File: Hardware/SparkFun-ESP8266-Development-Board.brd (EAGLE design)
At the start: 55.3 x 25.9 mm, 70 parts, among them J1 U.FL, Q1 2.5A/30V, Q2 MMBT2222A, U1 ESP8266, U2 MCP73831, U3 AT25SF041-SOIC8, U4 AP2112K-3.3V, U5 ATECC108-SSHDA, Y1 26MHz

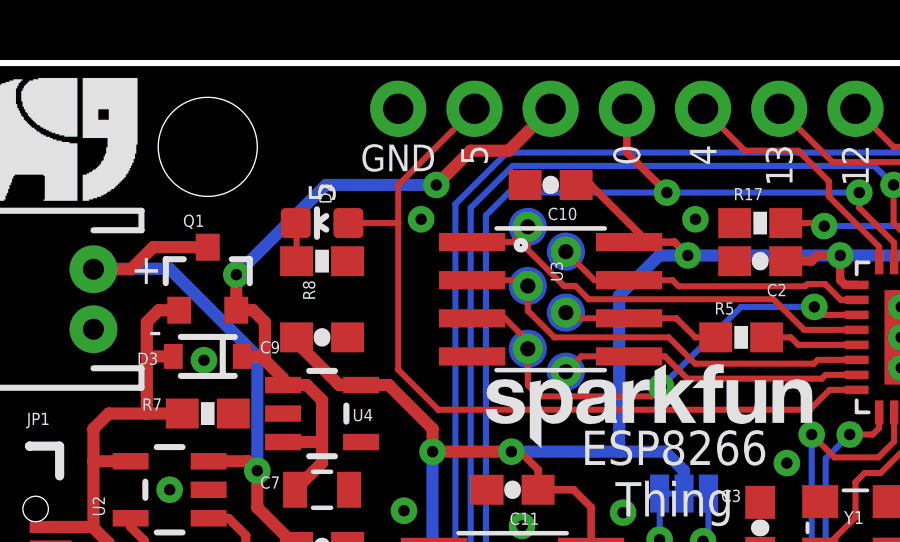
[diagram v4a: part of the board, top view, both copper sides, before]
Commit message: Re-arranging 10-pin header pin-out.
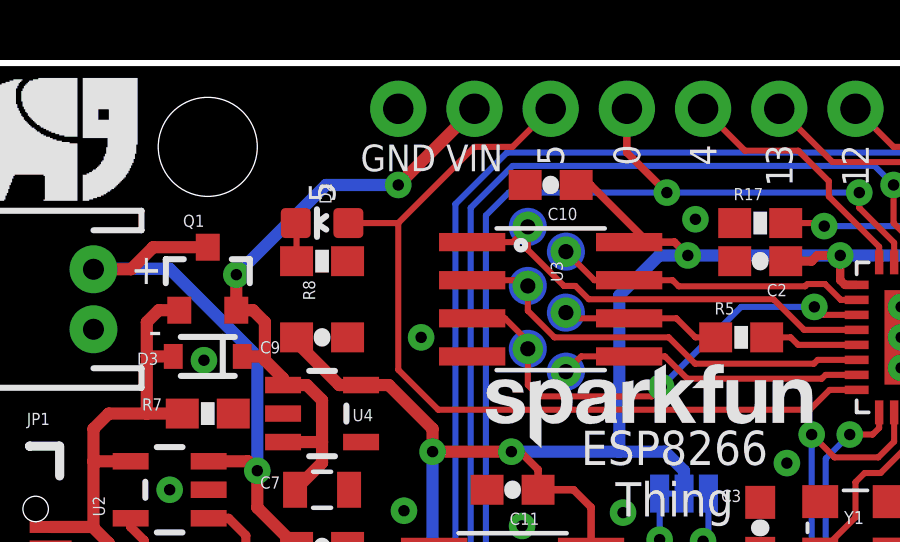
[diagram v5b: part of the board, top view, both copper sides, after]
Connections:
- net GPIO5: now also JP3.3; no longer JP3.2
- net VIN: now also JP3.2; no longer JP3.3
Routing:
- net VIN: track 24.3 -> 21.8 mm
- net GPIO5: track 27.5 -> 29.3 mm
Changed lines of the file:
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@@
 <text x="8.636" y="16.764" size="1.016" layer="21" font="vector" ratio="15" align="center-right">-</text>
 <text x="16.51" y="22.8092" size="0.889" layer="22" font="vector" ratio="15" rot="MR90" align="center-right">GND</text>
-<text x="21.59" y="22.6822" size="0.889" layer="22" font="vector" ratio="15" rot="MR0" align="top-center">VIN</text>
+<text x="19.05" y="22.6822" size="0.889" layer="22" font="vector" ratio="15" rot="MR0" align="top-center">VIN</text>
 <text x="24.13" y="22.8092" size="0.889" layer="22" font="vector" ratio="15" rot="MR90" align="center-right">0</text>
 <text x="26.67" y="22.8092" size="0.889" layer="22" font="vector" ratio="15" rot="MR90" align="center-right">4</text>
@@
 <text x="36.83" y="2.794" size="0.889" layer="22" font="vector" ratio="15" rot="MR90" align="center-left">NC</text>
 <text x="13.9954" y="5.6642" size="0.889" layer="21" font="vector" ratio="15" rot="R180" align="bottom-center">PWR</text>
-<text x="19.05" y="22.9362" size="0.889" layer="21" font="vector" ratio="15" rot="R90" align="center-right">5</text>
-<text x="19.05" y="22.8092" size="0.889" layer="22" font="vector" ratio="15" rot="MR90" align="center-right">5</text>
+<text x="21.59" y="22.8092" size="0.889" layer="22" font="vector" ratio="15" rot="MR90" align="center-right">5</text>
 <text x="13.97" y="21.0058" size="0.889" layer="21" font="vector" ratio="15" rot="R270" align="center-right">5</text>
+<text x="19.05" y="22.9362" size="0.889" layer="21" font="vector" ratio="15" align="top-center">VIN</text>
+<text x="21.59" y="22.9362" size="0.889" layer="21" font="vector" ratio="15" rot="R90" align="center-right">5</text>
 </plain>
 <attributes>
@@
 <via x="2.2225" y="5.1435" extent="1-16" drill="0.381"/>
 <via x="20.6375" y="10.2235" extent="1-16" drill="0.381"/>
-<via x="17.272" y="20.447" extent="1-16" drill="0.381"/>
+<via x="17.272" y="16.51" extent="1-16" drill="0.381"/>
 <via x="27.8511" y="5.5245" extent="1-16" drill="0.381"/>
 <contactref element="E1" pad="GND"/>
@@
 <wire x1="16.51" y1="15.4305" x2="16.51" y2="20.32" width="0.2032" layer="1"/>
 <wire x1="14.847" y1="20.32" x2="16.51" y2="20.32" width="0.2032" layer="1"/>
-<contactref element="JP3" pad="2"/>
-<wire x1="16.51" y1="20.32" x2="16.51" y2="21.59" width="0.2032" layer="1"/>
-<wire x1="16.51" y1="21.59" x2="19.05" y2="24.13" width="0.2032" layer="1"/>
+<contactref element="JP3" pad="3"/>
+<wire x1="16.51" y1="20.32" x2="19.05" y2="22.86" width="0.2032" layer="1"/>
+<wire x1="19.05" y1="22.86" x2="20.32" y2="22.86" width="0.2032" layer="1"/>
+<wire x1="20.32" y1="22.86" x2="21.59" y2="24.13" width="0.2032" layer="1"/>
 </signal>
 <signal name="GPIO4">
@@
 <wire x1="12.6699" y1="13.02" x2="13.97" y2="13.02" width="0.4064" layer="1"/>
 <wire x1="13.97" y1="13.02" x2="13.97" y2="14.4145" width="0.4064" layer="1"/>
-<wire x1="17.78" y1="21.59" x2="14.102" y2="21.59" width="0.4064" layer="16"/>
+<wire x1="16.51" y1="21.59" x2="14.102" y2="21.59" width="0.4064" layer="16"/>
 <contactref element="U4" pad="1"/>
 <contactref element="U4" pad="3"/>
@@
 <wire x1="13.97" y1="13.02" x2="13.97" y2="12.33" width="0.4064" layer="1"/>
 <wire x1="13.97" y1="12.33" x2="13.07" y2="11.43" width="0.4064" layer="1"/>
-<contactref element="JP3" pad="3"/>
-<via x="17.78" y="21.59" extent="1-16" drill="0.381"/>
-<wire x1="17.78" y1="21.59" x2="18.923" y2="22.733" width="0.4064" layer="1"/>
-<wire x1="18.923" y1="22.733" x2="20.193" y2="22.733" width="0.4064" layer="1"/>
-<wire x1="20.193" y1="22.733" x2="21.59" y2="24.13" width="0.4064" layer="1"/>
+<via x="16.51" y="21.59" extent="1-16" drill="0.381"/>
+<contactref element="JP3" pad="2"/>
+<wire x1="19.05" y1="24.13" x2="16.51" y2="21.59" width="0.4064" layer="1"/>
 </signal>
 <signal name="VUSB">

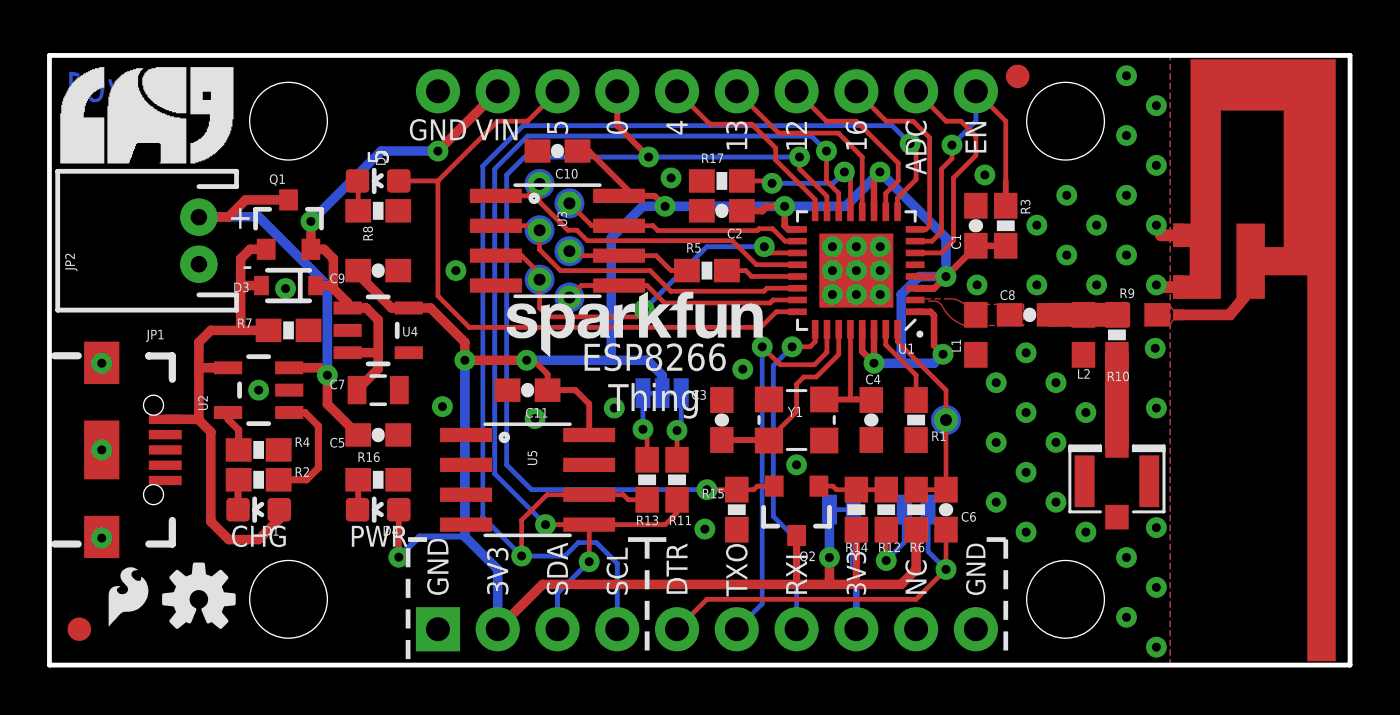
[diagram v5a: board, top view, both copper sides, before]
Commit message: Adding light and temperature sensors. Adding ON/OFF switch. Simplifying DTR-GPIO0 circuit.
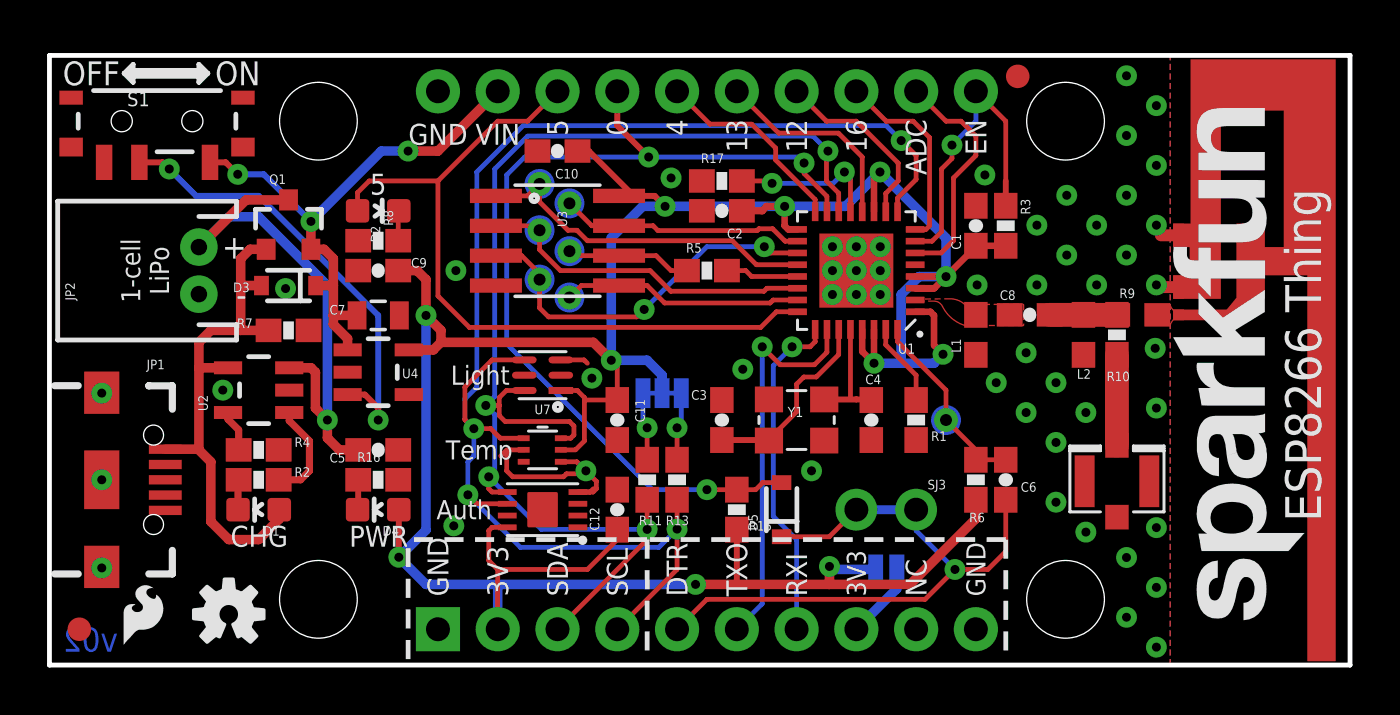
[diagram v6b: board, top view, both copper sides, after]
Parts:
- removed LOGO2: SFE_LOGO_NAME.1_INCH, SparkFun-Aesthetics:SFE_LOGO_NAME_.1
- removed Q2: MMBT2222A, SparkFun-DiscreteSemi:SOT23-3
- removed R12: 200, SparkFun-Resistors:0603-RES
- removed R14: 1K, SparkFun-Resistors:0603-RES
- removed SJ1: PROG, SparkFun-Passives:PAD-JUMPER-2-NC_BY_TRACE_YES_SILK
- added C12: 0.1uF, SparkFun-Capacitors:0603-CAP
- added D5: (no value), SparkFun-DiscreteSemi:SOD-323
- added LOGO5: SFE_LOGO_NAME.2_INCH, SparkFun-Aesthetics:SFE_LOGO_NAME_.2
- added S1: (no value), SparkFun-Electromechanical:SWITCH-SPST-SMD-A
- added SJ4: (no value), SparkFun-Passives:PAD-JUMPER-2-NO_YES_SILK
- added U6: TMP1021:1, SparkFun-Sensors:SOT563-2
- added U7: TSL2561FN, esp8266-development-board:FN-6
- JP2: value M02JST-PTH-2 -> LiPo
- LOGO1: value SFE_LOGO_NAME.1_INCH -> SFE_LOGO_NAME.2_INCH; device SparkFun-Aesthetics:SFE_LOGO_NAME_.1 -> SparkFun-Aesthetics:SFE_LOGO_NAME_.2
- SJ3: value FTDI_VCC -> (none); device SparkFun-Passives:PAD-JUMPER-2-NC_BY_TRACE_YES_SILK -> SparkFun-Passives:PTH-JUMPER-NC_BOTTOM_NO_SILK
- U5: value ATECC108-SSHDA -> ATECC108-MAHDA; device esp8266-development-board:SO08 -> esp8266-development-board:UDFN8
- moved LOGO1 28.1 mm to (49.3, 1.65), turned to 90 degrees
- moved C11 4.02 mm to (24.1, 10.2), turned to 270 degrees
- moved C7 3.18 mm to (14.0, 14.6)
- moved C6 2.84 mm to (40.6, 7.62)
- moved R6 2.84 mm to (39.4, 7.62)
- moved SJ3 1.91 mm to (35.6, 6.35), flipped to the top, turned to 180 degrees
- moved U4 1.78 mm to (14.0, 12.2)
- moved LOGO4 1.42 mm to (7.62, 1.91)
- moved U5 1.42 mm to (21.0, 6.35), turned to 180 degrees
- moved R11 1.27 mm to (25.4, 7.62)
- moved R13 1.27 mm to (26.7, 7.62)
- moved JP1 1.27 mm to (2.22, 7.62)
- moved D2 1.27 mm to (14.0, 19.1), turned to 270 degrees
- moved JP2 1.27 mm to (6.35, 16.5)
- moved R8 1.27 mm to (14.0, 17.8), turned to 180 degrees
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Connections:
- removed net N$8: R12.2, SJ1.2
- new net N$11: S1.2, U4.3
- net DTR: now also SJ3.1; no longer SJ1.1
- net FTDI_VCC: now also SJ4.1; no longer SJ3.1
- net GND: now also C12.2, S1.1, U6.2, U6.4, U7.2, U7.3; no longer R15.1
- net GPIO0: now also D5.A, R15.1; no longer Q2.2, R15.2
- net GPIO14/SCL: now also U6.1, U7.4
- net GPIO2/SDA: now also U6.6, U7.6
- net N$10: now also SJ2.3; no longer SJ2.1
- net N$7: now also D5.C, SJ3.2; no longer Q2.1, R12.1, R14.1
- net N$9: now also SJ2.1; no longer SJ2.3
- net VCC: now also C12.1, R15.2, SJ4.2, U6.5, U7.1; no longer Q2.3, R14.2, SJ3.2
- net VIN: now also S1.3; no longer U4.3
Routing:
- net N$11: track 0.00 -> 19.3 mm, vias 0 -> 2
- net VCC: track 121.1 -> 136.4 mm, vias 10 -> 11
- net GND: track 1.80 -> 12.2 mm, vias 57 -> 52
- net GPIO2/SDA: track 45.1 -> 54.3 mm, vias 3 -> 4
- net GPIO14/SCL: track 54.6 -> 62.7 mm, vias 2 -> 4
- net VBAT: track 19.4 -> 23.3 mm
- net N$8: track 3.78 -> 0.00 mm, vias 1 -> 0
- net DTR: track 17.0 -> 20.8 mm
- net GPIO5: track 29.3 -> 32.1 mm
- net GPIO0: track 43.1 -> 40.4 mm
- net VIN: track 21.8 -> 23.8 mm, vias 2 -> 3
- net FTDI_VCC: track 5.13 -> 3.25 mm
- net N$18: track 5.16 -> 4.30 mm
- net RESET: track 8.93 -> 8.19 mm
- net N$7: track 2.92 -> 3.65 mm
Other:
- board text added: "1-cell LiPo"
- board text added: "Auth"
- board text added: "Light"
- board text added: "OFF"
- board text added: "ON"
- board text added: "Temp"
- board text added: "data.sparkfun.com"
- board text added: "v02"
- board text removed: "v01"

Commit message: Swapping colors of PWR and pin 5 LEDs. Adding SMD jumper to GPIO0/DTR.
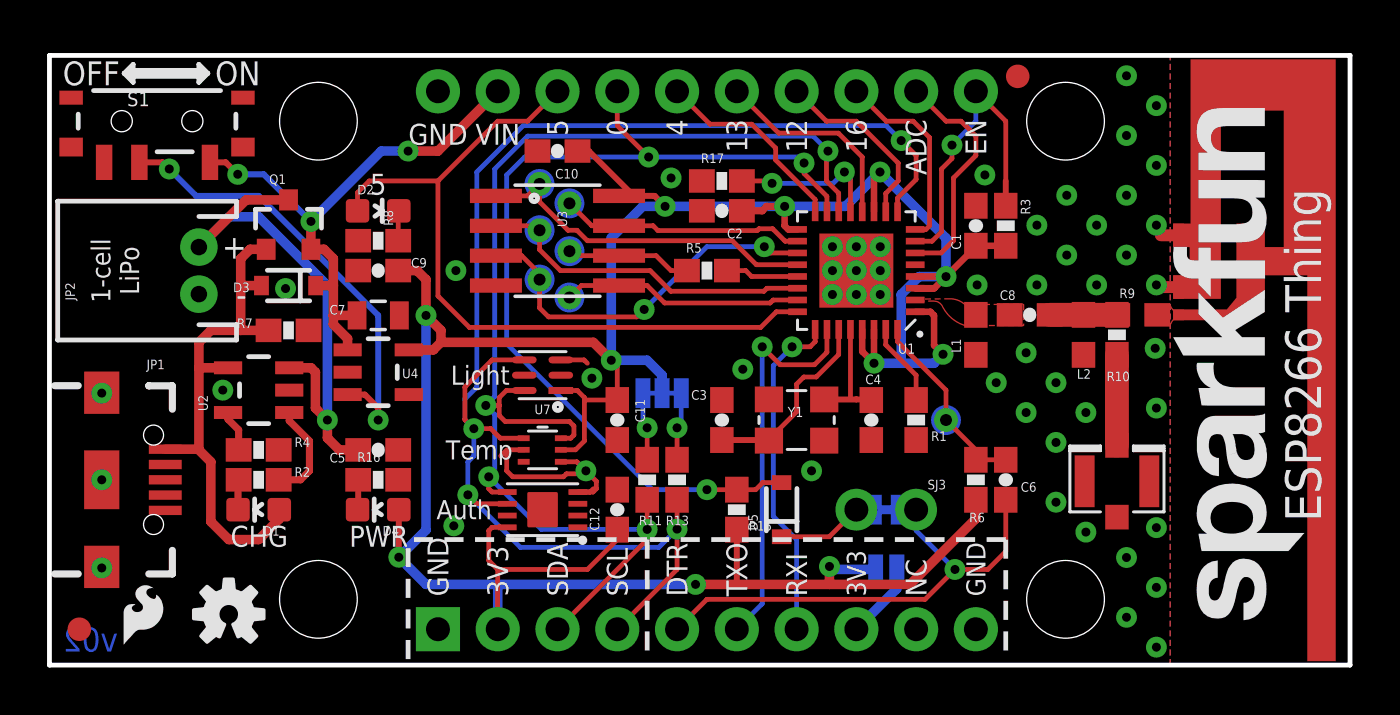
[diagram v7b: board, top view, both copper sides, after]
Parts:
- added SJ1: (no value), SparkFun-Passives:PAD-JUMPER-2-NC_BY_TRACE_YES_SILK
- D2: value RED -> GREEN
- D4: value GREEN -> RED
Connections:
- net DTR: now also SJ1.2
- net N$7: now also SJ1.1
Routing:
- net N$7: track 3.65 -> 4.41 mm
- net DTR: track 20.8 -> 21.5 mm
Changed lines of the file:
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@@
 <layer number="47" name="Measures" color="7" fill="1" visible="no" active="yes"/>
 <layer number="48" name="Document" color="7" fill="1" visible="no" active="yes"/>
-<layer number="49" name="Reference" color="7" fill="1" visible="yes" active="yes"/>
+<layer number="49" name="Reference" color="7" fill="1" visible="no" active="yes"/>
 <layer number="50" name="dxf" color="7" fill="1" visible="no" active="no"/>
 <layer number="51" name="tDocu" color="6" fill="1" visible="yes" active="yes"/>
@@
 <wire x1="3.683" y1="25.019" x2="6.223" y2="25.019" width="0.2032" layer="21"/>
 <wire x1="6.223" y1="24.765" x2="3.683" y2="24.765" width="0.2032" layer="21"/>
-<text x="5.08" y="16.51" size="0.8128" layer="21" font="vector" ratio="15" rot="R90" align="bottom-center">1-cell
+<text x="3.81" y="16.51" size="0.8128" layer="21" font="vector" ratio="15" rot="R90" align="bottom-center">1-cell
 LiPo</text>
 </plain>
@@
 <attribute name="VALUE" x="7.366" y="6.5405" size="0.4064" layer="27" rot="R180"/>
 </element>
-<element name="D2" library="SparkFun-LED" package="LED-0603" value="RED" x="13.97" y="19.05" smashed="yes" rot="R270">
-<attribute name="PROD_ID" value="DIO-00819" x="13.97" y="19.05" size="1.778" layer="27" font="vector" ratio="15" rot="R270" display="off"/>
-<attribute name="NAME" x="13.6525" y="18.415" size="0.4064" layer="25" rot="R270"/>
-<attribute name="VALUE" x="13.0175" y="18.415" size="0.4064" layer="27" rot="R270"/>
-</element>
 <element name="TP7" library="SparkFun-Passives" package="PAD.03X.05" value="" x="38.1" y="10.16" rot="MR0"/>
 <element name="LOGO1" library="SparkFun-Aesthetics" package="SFE_LOGO_NAME_.2" value="SFE_LOGO_NAME.2_INCH" x="49.276" y="1.651" rot="MR90"/>
@@
 <attribute name="PROD_ID" value="TRANS-11308" x="10.16" y="18.415" size="1.016" layer="27" font="vector" ratio="15" display="off"/>
 </element>
-<element name="D4" library="SparkFun-LED" package="LED-0603" value="GREEN" x="13.97" y="6.35" rot="R90">
-<attribute name="PROD_ID" value="DIO-00821" x="13.97" y="6.35" size="1.016" layer="27" font="vector" ratio="15" rot="R90" display="off"/>
-</element>
 <element name="R16" library="SparkFun-Resistors" package="0603-RES" value="200" x="13.97" y="7.62">
 <attribute name="PROD_ID" value="RES-08220" x="13.97" y="7.62" size="1.016" layer="27" font="vector" ratio="15" display="off"/>
@@
 <attribute name="PROD_ID" value="CAP-00810" x="24.13" y="6.35" size="0.8128" layer="27" font="vector" ratio="15" rot="R90" display="off"/>
 </element>
+<element name="D4" library="SparkFun-LED" package="LED-0603" value="RED" x="13.97" y="6.35" rot="R90">
+<attribute name="PROD_ID" value="DIO-00819" x="13.97" y="6.35" size="0.8128" layer="27" font="vector" ratio="15" rot="R90" display="off"/>
+</element>
+<element name="D2" library="SparkFun-LED" package="LED-0603" value="GREEN" x="13.97" y="19.05" rot="R270">
+<attribute name="PROD_ID" value="DIO-00821" x="13.97" y="19.05" size="0.8128" layer="27" font="vector" ratio="15" rot="R270" display="off"/>
+</element>
+<element name="SJ1" library="SparkFun-Passives" package="PAD-JUMPER-2-NC_BY_TRACE_YES_SILK" value="" x="35.56" y="6.35" rot="MR180"/>
 </elements>
 <signals>
@@
 <wire x1="23.876" y1="17.907" x2="25.2095" y2="19.2405" width="0.4064" layer="16"/>
 <wire x1="25.2095" y1="19.2405" x2="26.162" y2="19.2405" width="0.4064" layer="16"/>
-<contactref element="D4" pad="A"/>
 <wire x1="14.847" y1="6.35" x2="14.847" y2="4.33" width="0.254" layer="1"/>
 <via x="14.847" y="4.33" extent="1-16" drill="0.381"/>
@@
 <wire x1="22.86" y1="3.81" x2="19.05" y2="3.81" width="0.2032" layer="1"/>
 <wire x1="24.13" y1="11.01" x2="22.733" y2="11.01" width="0.2032" layer="1"/>
+<contactref element="D4" pad="A"/>
 </signal>
 <signal name="GND">
@@
 <wire x1="40.64" y1="4.572" x2="39.878" y2="3.81" width="0.2032" layer="1"/>
 <wire x1="39.878" y1="3.81" x2="38.481" y2="3.81" width="0.2032" layer="1"/>
+<contactref element="SJ1" pad="2"/>
+<wire x1="36.068" y1="6.35" x2="36.83" y2="6.35" width="0.2032" layer="16"/>
 </signal>
 <signal name="GPIO14/SCL">
@@
 <wire x1="25.4635" y1="21.336" x2="20.193" y2="21.336" width="0.2032" layer="16"/>
 <wire x1="20.193" y1="21.336" x2="19.431" y2="20.574" width="0.2032" layer="16"/>
-<wire x1="24.13" y1="22.6695" x2="25.4635" y2="21.336" width="0.254" layer="1"/>
+<wire x1="24.13" y1="22.6695" x2="25.4635" y2="21.336" width="0.2032" layer="1"/>
 <contactref element="JP3" pad="4"/>
-<wire x1="24.13" y1="24.13" x2="24.13" y2="22.6695" width="0.254" layer="1"/>
+<wire x1="24.13" y1="24.13" x2="24.13" y2="22.6695" width="0.2032" layer="1"/>
 <wire x1="33.04" y1="19.01" x2="33.04" y2="19.665" width="0.2032" layer="1"/>
 <wire x1="27.94" y1="7.2" x2="25.6295" y2="7.2" width="0.2032" layer="16"/>
@@
 <signal name="GPIO5">
 <contactref element="U1" pad="24"/>
-<contactref element="D2" pad="A"/>
 <wire x1="31.79" y1="14.76" x2="30.889" y2="14.76" width="0.2032" layer="1"/>
 <wire x1="30.889" y1="14.76" x2="30.226" y2="14.097" width="0.2032" layer="1"/>
@@
 <wire x1="13.093" y1="19.824" x2="13.589" y2="20.32" width="0.2032" layer="1"/>
 <wire x1="13.589" y1="20.32" x2="16.51" y2="20.32" width="0.2032" layer="1"/>
+<contactref element="D2" pad="A"/>
 </signal>
 <signal name="GPIO4">
@@
 </signal>
 <signal name="N$15">
-<contactref element="D2" pad="C"/>
 <contactref element="R8" pad="1"/>
 <wire x1="14.82" y1="17.78" x2="14.82" y2="19.023" width="0.2032" layer="1"/>
 <wire x1="14.82" y1="19.023" x2="14.847" y2="19.05" width="0.2032" layer="1"/>
+<contactref element="D2" pad="C"/>
 </signal>
 <signal name="ANT">
@@
 </signal>
 <signal name="N$4">
-<contactref element="D4" pad="C"/>
 <contactref element="R16" pad="1"/>
 <wire x1="13.12" y1="7.62" x2="13.12" y2="6.377" width="0.254" layer="1"/>
 <wire x1="13.12" y1="6.377" x2="13.093" y2="6.35" width="0.254" layer="1"/>
+<contactref element="D4" pad="C"/>
 </signal>
 <signal name="N$7">
@@
 <wire x1="31.115" y1="5.2" x2="33.14" y2="5.2" width="0.2032" layer="1"/>
 <wire x1="33.14" y1="5.2" x2="34.29" y2="6.35" width="0.2032" layer="1"/>
+<contactref element="SJ1" pad="1"/>
+<wire x1="35.052" y1="6.35" x2="34.29" y2="6.35" width="0.2032" layer="16"/>
 </signal>
 <signal name="N$11">
